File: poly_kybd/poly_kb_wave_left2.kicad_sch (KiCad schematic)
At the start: 47 parts, among them J37 FH34SRJ-12S-0.5SH, J38 Conn_01x05, J39 FH12-30S-0.5SH, SW1 RotaryEncoder_Switch, U2 TD6811, U3 MT9700

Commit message: Update PCB and plate to rev3 (disconnected vbus via bridge and removed polyfuse)
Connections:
- net VBUS: no longer USB2.11 (VBUS), USB2.2 (VBUS)
- net VSYS: now also USB2.11 (VBUS), USB2.2 (VBUS)
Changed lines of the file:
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@@
   (title_block
     (title "PolyKybd Split R")
-    (date "2023-06-22")
-    (rev "2.2")
+    (date "2023-09-19")
+    (rev "3")
   )
   (junction (at 259.08 219.075) (diameter 0) (color 0 0 0 0)
@@
     )
   )
-  (global_label "VBUS" (shape input) (at 410.21 358.14 0) (fields_autoplaced)
+  (global_label "VSYS" (shape input) (at 410.21 358.14 0) (fields_autoplaced)
     (effects (font (size 1.27 1.27)) (justify left))
-    (property "Intersheetrefs" "${INTERSHEET_REFS}" (at 417.5217 358.0606 0)
+    (property "Intersheetrefs" "${INTERSHEET_REFS}" (at 417.7914 358.14 0)
       (effects (font (size 1.27 1.27)) (justify left) hide)
     )
@@
     )
   )
-  (global_label "VBUS" (shape input) (at 410.21 381 0) (fields_autoplaced)
+  (global_label "VSYS" (shape input) (at 410.21 381 0) (fields_autoplaced)
     (effects (font (size 1.27 1.27)) (justify left))
-    (property "Intersheetrefs" "${INTERSHEET_REFS}" (at 417.5217 380.9206 0)
+    (property "Intersheetrefs" "${INTERSHEET_REFS}" (at 417.7914 381 0)
       (effects (font (size 1.27 1.27)) (justify left) hide)
     )

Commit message: Added latest gerber files, latest STLs and updated readme
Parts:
- R13: value 22k 0603 -> 12k 0603; JLC (none) -> C22790; MPN C31850 -> C22790
- R25: value 5.1K 0402 -> 10K 0402; MPN C25905 -> C25744
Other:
- note added: "Rset 27k -> ~250mA Max / Rset 22k -> ~310mA Max"
- note removed: "~250mA Max"
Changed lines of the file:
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@@
     (effects (font (size 3 3) (thickness 0.6) bold) (justify left bottom))
   )
-  (text "Increase for more current: Imax = 6.8k / RSet" (at 504.19 374.015 0)
+  (text "Increase for more current: Imax = 6.8k / RSet" (at 510.54 372.11 0)
     (effects (font (size 1.27 1.27) bold) (justify left bottom))
   )
@@
     (effects (font (size 3 3) (thickness 0.6) bold) (justify left bottom))
   )
-  (text "~250mA Max" (at 554.99 349.25 0)
-    (effects (font (size 1.27 1.27)) (justify left bottom))
-  )
   (text "Display Charge Pump Power Supply VBAT" (at 474.345 280.67 0)
     (effects (font (size 3 3) (thickness 0.6) bold) (justify left bottom))
@@
     (effects (font (size 3 3) (thickness 0.6) bold) (justify left bottom))
   )
+  (text "Rset 27k -> ~250mA Max / Rset 22k -> ~310mA Max" (at 499.745 375.285 0)
+    (effects (font (size 1.27 1.27)) (justify left bottom))
+  )
   (label "SCLK6" (at 290.83 30.48 0) (fields_autoplaced)
     (effects (font (size 1.27 1.27)) (justify left bottom))
@@
       (effects (font (size 1.27 1.27)))
     )
-    (property "Value" "5.1K 0402" (at 490.855 369.57 90)
+    (property "Value" "10K 0402" (at 490.855 369.57 90)
       (effects (font (size 1.27 1.27)))
     )
@@
       (effects (font (size 1.27 1.27)) hide)
     )
-    (property "MPN" "C25905" (at 492.76 363.22 0)
+    (property "MPN" "C25744" (at 492.76 363.22 0)
       (effects (font (size 1.27 1.27)) hide)
     )
@@
       (effects (font (size 1.27 1.27)))
     )
-    (property "Value" "22k 0603" (at 503.555 369.57 90)
+    (property "Value" "12k 0603" (at 503.555 369.57 90)
       (effects (font (size 1.27 1.27)))
     )
@@
       (effects (font (size 1.27 1.27)) hide)
     )
-    (property "MPN" "C31850" (at 501.015 363.22 0)
+    (property "MPN" "C22790" (at 501.015 363.22 0)
       (effects (font (size 1.27 1.27)) hide)
     )
-    (property "JLC" "" (at 501.015 363.22 0)
+    (property "JLC" "C22790" (at 501.015 363.22 0)
       (effects (font (size 1.27 1.27)) hide)
     )

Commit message: Revision D caps and schematics part cleanup
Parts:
- C10, C12, C13, C14: JLC (none) -> C15850; LCSC (none) -> C15850
- C11: JLC (none) -> C1653; LCSC (none) -> C1653
- C2, C30, C31, C32: JLC (none) -> C52923; LCSC (none) -> C52923
- C33, C34: JLC (none) -> C129569; LCSC (none) -> C129569
- D12: JLC (none) -> C2128; LCSC (none) -> C2128
- D5: JLC (none) -> C2297; LCSC (none) -> C2297
- D6: JLC (none) -> C2296; LCSC (none) -> C2296
- DBG1, DBG3, H1, H2, H3, H4, H5, H6, H7, H8, H9, J38, JP1, SW1: JLC (none) -> DNP; LCSC (none) -> DNP; MPN (none) -> DNP
- FB2: JLC (none) -> C1017; LCSC (none) -> C1017
- J37: JLC (none) -> C424659; LCSC (none) -> C424659
- J39: JLC (none) -> C506793; LCSC (none) -> C506793
- L1: JLC (none) -> C2836880; LCSC (none) -> C2836880
- R1, R2: JLC (none) -> C23345; LCSC (none) -> C23345
- R10, R11, R30: JLC (none) -> C23150; LCSC (none) -> C23150
- R12: JLC (none) -> C22807; LCSC (none) -> C22807
- R13: LCSC (none) -> C22790
- R25: JLC (none) -> C25744; LCSC (none) -> C25744
- R3, R4: JLC (none) -> C25905; LCSC (none) -> C25905
- R5, R6: JLC (none) -> C21190; LCSC (none) -> C21190
- U2: JLC (none) -> C189486; LCSC (none) -> C189486
- U3: JLC (none) -> C89855; LCSC (none) -> C89855
- USB2: JLC (none) -> C165948; LCSC (none) -> C165948

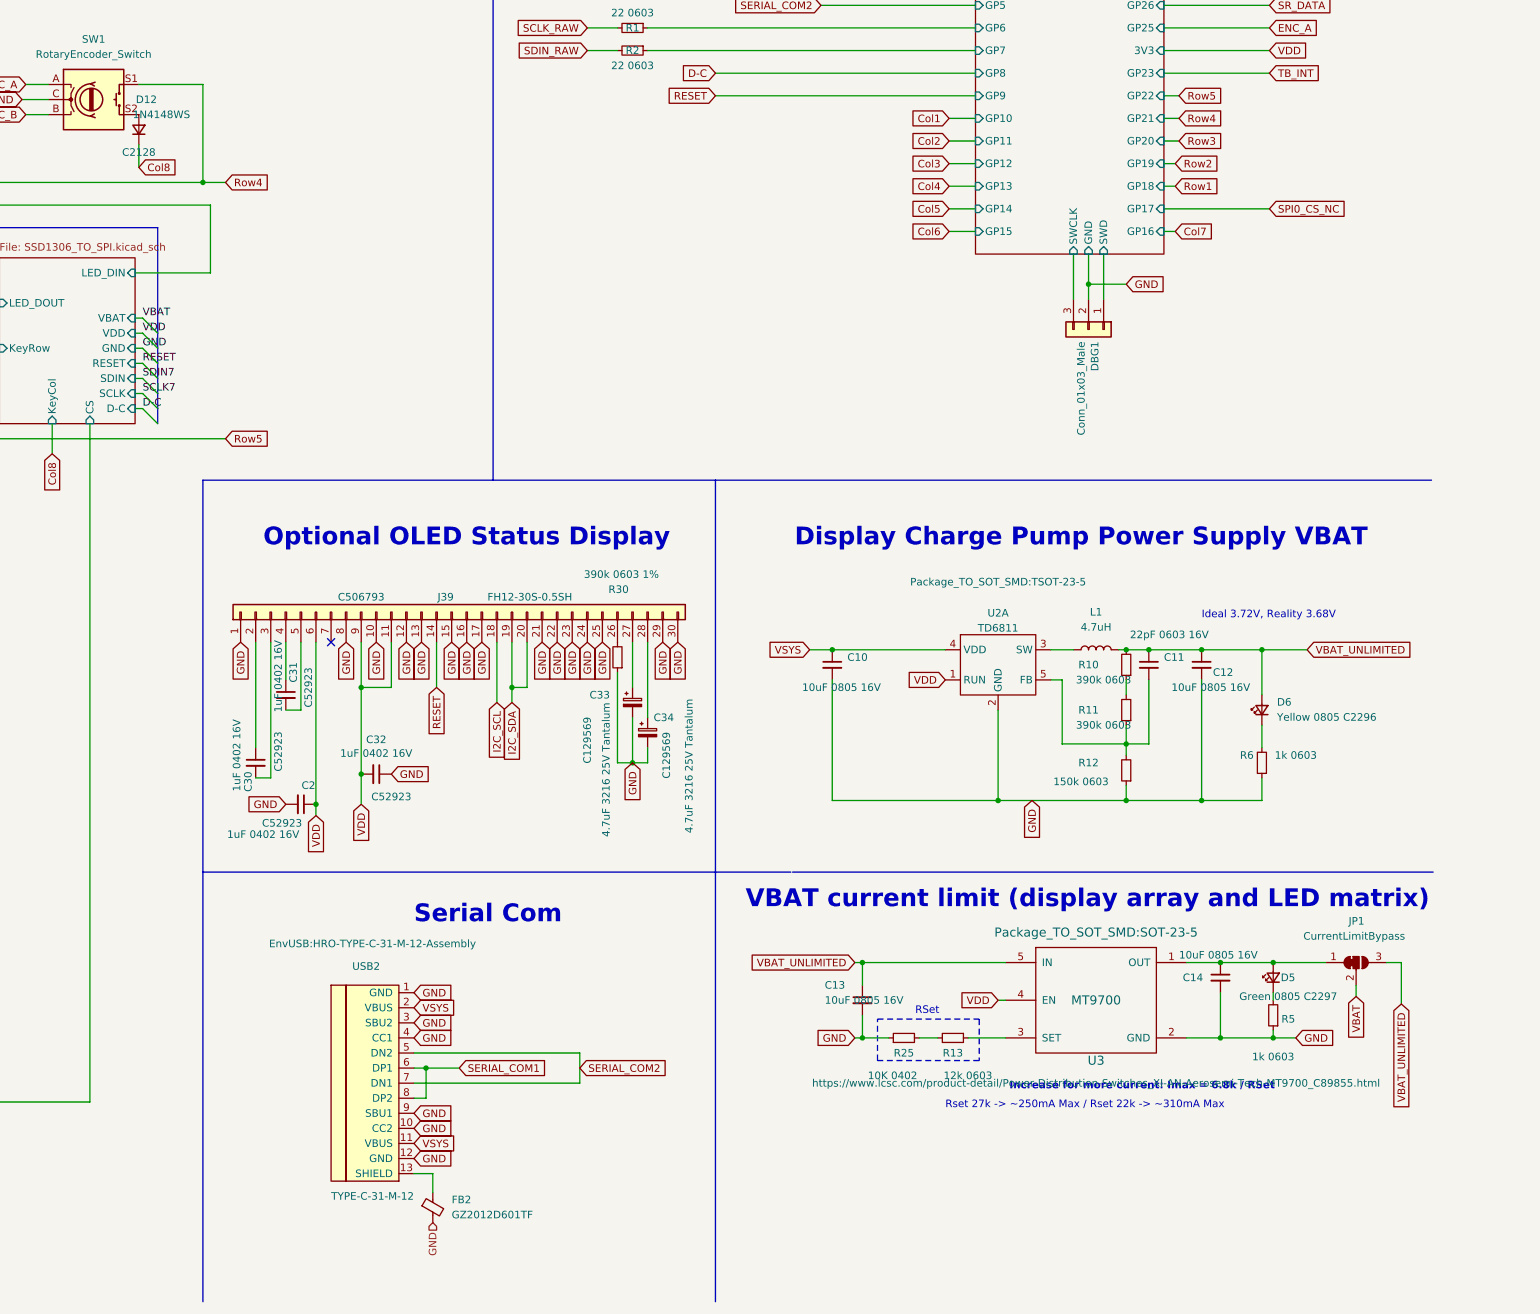
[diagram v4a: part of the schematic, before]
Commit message: Updated left side for RoHS
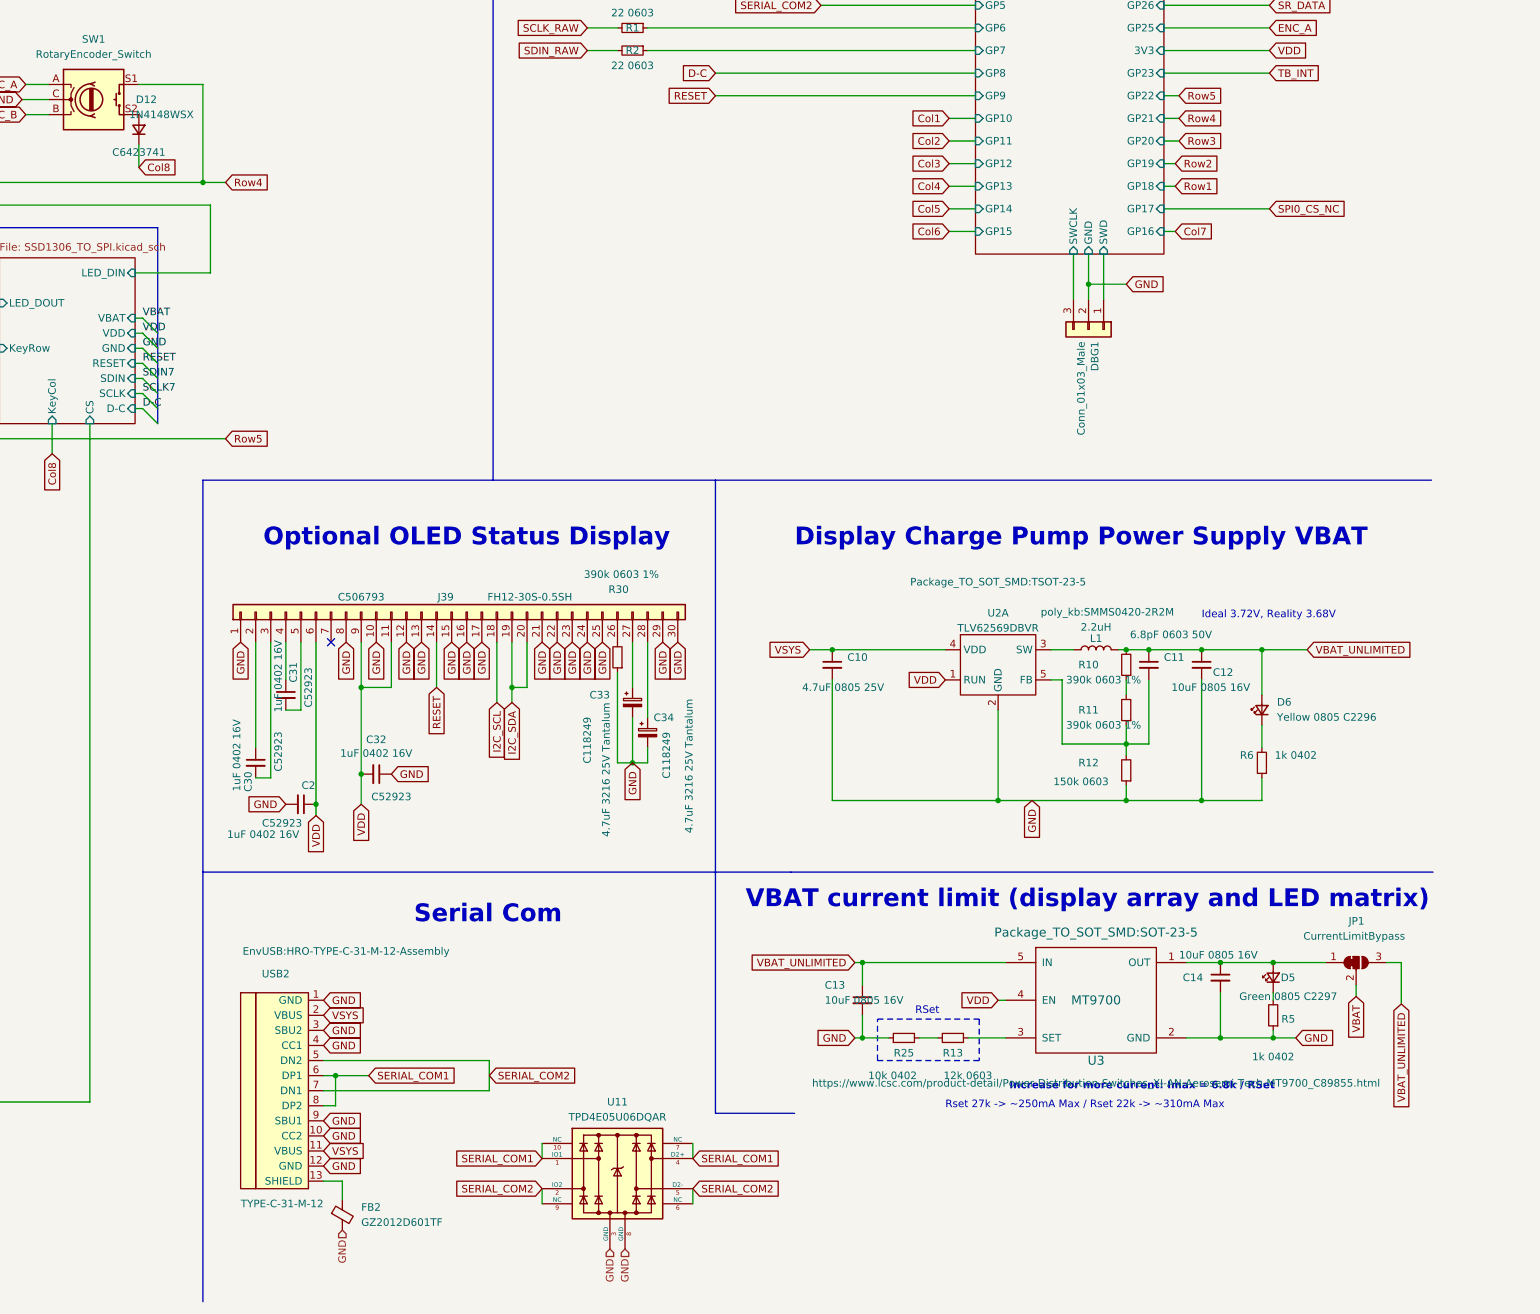
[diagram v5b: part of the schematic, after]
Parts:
- added U11: TPD4E05U06DQAR, poly_kb:USON-10, symbol acheron_Symbols:TPD4E05U06DQAR
- C10: value 10uF 0805 16V -> 4.7uF 0805 25V; JLC C15850 -> C1779; LCSC C15850 -> C1779; MPN C15850 -> C1779; Manufacturer (none) -> Samsung; RoHS (none) -> x
- C11: value 22pF 0603 16V -> 6.8pF 0603 50V; JLC C1653 -> C170128; LCSC C1653 -> C170128; MPN C1653 -> C170128; Manufacturer (none) -> Samsung; RoHS (none) -> x
- C12, C13, C14, C2, C30, C31, C32: Manufacturer (none) -> Samsung; RoHS (none) -> x
- C33, C34: Etc (none) -> Preorder Req; JLC C129569 -> C118249; LCSC C129569 -> C118249; MPN C129569 -> C118249; Manufacturer (none) -> Sunlord; RoHS (none) -> x
- D12: value 1N4148WS -> 1N4148WSX; JLC C2128 -> C6423741; LCSC C2128 -> C6423741; MPN C2128 -> C6423741; Manufacturer (none) -> Shenzhen JingYang; RoHS (none) -> x
- D5, D6: Manufacturer (none) -> Hubei KENTO; RoHS (none) -> x
- FB2: Manufacturer (none) -> Sunlord; RoHS (none) -> x
- J37, J39: Manufacturer (none) -> Hirose; RoHS (none) -> x
- L1: value 4.7uH -> 2.2uH; footprint poly_kb:MCS0530-4R7MN2 -> poly_kb:SMMS0420-2R2M; JLC C2836880 -> C133191; LCSC C2836880 -> C133191; MPN C2836880 -> C133191; Manufacturer (none) -> SXN; RoHS (none) -> x
- R1, R2: JLC C23345 -> C108405; LCSC C23345 -> C108405; MPN C23345 -> C108405; Manufacturer (none) -> Yageo; RoHS (none) -> x
- R10, R11: value 390k 0603 -> 390k 0603 1%; JLC C23150 -> C137735; LCSC C23150 -> C137735; MPN C23150 -> C137735; Manufacturer (none) -> Yageo; RoHS (none) -> x
- R12: JLC C22807 -> C114660; LCSC C22807 -> C114660; MPN C22807 -> C114660; Manufacturer (none) -> Yageo; RoHS (none) -> x
- R13: JLC C22790 -> C114659; LCSC C22790 -> C114659; MPN C22790 -> C114659; Manufacturer (none) -> Yageo; RoHS (none) -> x
- R25: value 10K 0402 -> 10k 0402; JLC C25744 -> C60490; LCSC C25744 -> C60490; MPN C25744 -> C60490; Manufacturer (none) -> Yageo; RoHS (none) -> x
- R3, R4: JLC C25905 -> C144745; LCSC C25905 -> C144745; MPN C25905 -> C144745; Manufacturer (none) -> Yageo; RoHS (none) -> x
- R30: JLC C23150 -> C137735; LCSC C23150 -> C137735; MPN C23150 -> C137735; Manufacturer (none) -> Yageo; RoHS (none) -> x
- R5, R6: value 1k 0603 -> 1k 0402; footprint Resistor_SMD:R_0603_1608Metric -> Resistor_SMD:R_0402_1005Metric; JLC C21190 -> C144789; LCSC C21190 -> C144789; MPN C21190 -> C144789; Manufacturer (none) -> Yageo; RoHS (none) -> x
- U2: value TD6811 -> TLV62569DBVR; Etc (none) -> Replaced C189486 with C141836 (TI) (alt C222072 (ST)); JLC C189486 -> C141836; LCSC C189486 -> C141836; MPN C189486 -> C141836; Manufacturer (none) -> TI; RoHS (none) -> x
- U3: Etc (none) -> Email sent; Alternative C55136 is RoHS; Manufacturer (none) -> XI'AN Aerosemi Tech; RoHS (none) -> Email sent
- USB2: Manufacturer (none) -> Hroparts; RoHS (none) -> x
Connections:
- net GND: now also U11.3 (GND), U11.8 (GND)
- net SERIAL_COM1: now also U11.1 (IO1), U11.10 (NC), U11.4 (D2+), U11.7 (NC)
- net SERIAL_COM2: now also U11.2 (IO2), U11.5 (D2-), U11.6 (NC), U11.9 (NC)
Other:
- title: PolyKybd Split R -> PolyKybd Split L
- moved on the sheet: FB2, USB2
